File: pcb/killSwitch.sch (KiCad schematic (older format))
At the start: 8 parts

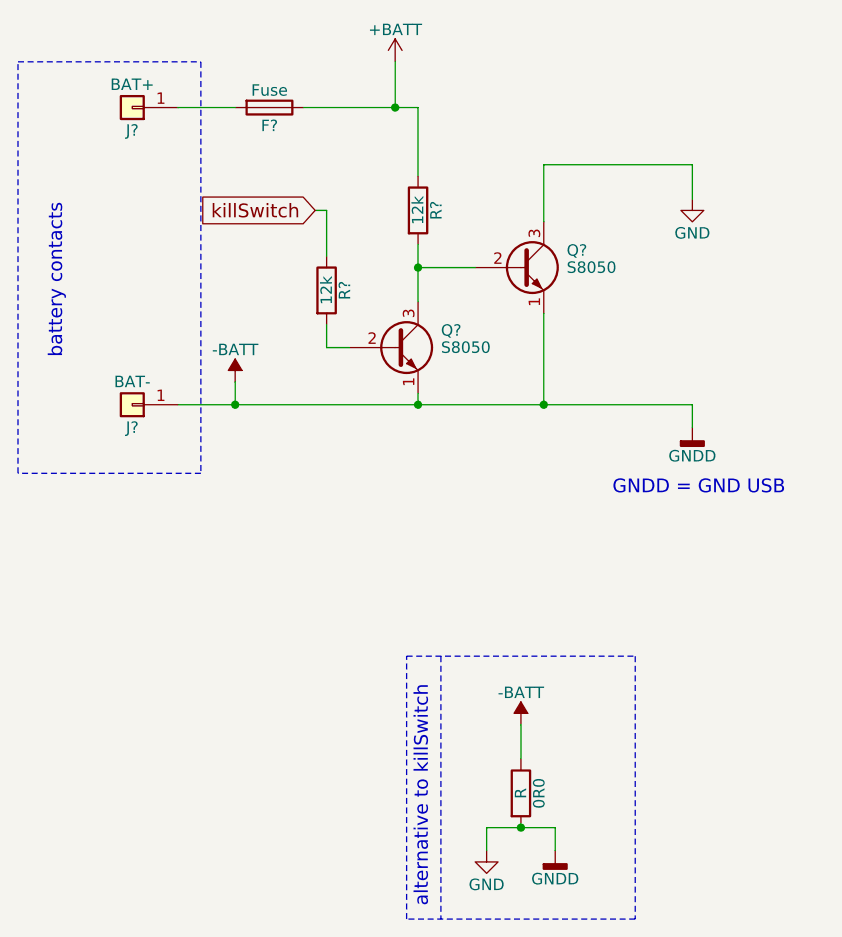
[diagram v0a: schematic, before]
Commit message: nightly | pcb build, routing, placing
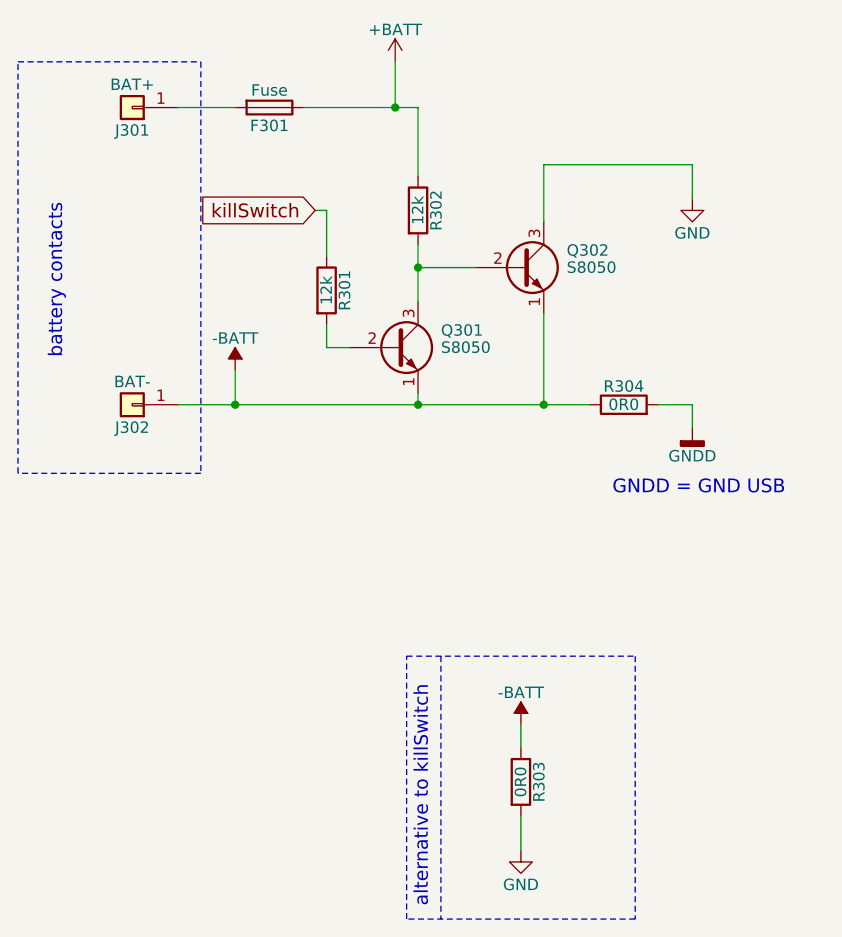
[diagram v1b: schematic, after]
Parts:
- added R304: 0R0, Resistors_SMD:R_0603_HandSoldering, symbol R
- F301: renamed from F?; footprint (none) -> SMD_Packages:SMD-1210_Pol
- J301, J302: renamed from J?; footprint (none) -> Wire_Pads:SolderWirePad_single_SMD_5x10mm
- Q301, Q302: renamed from Q?; footprint TO_SOT_Packages_THT:TO-92_Molded_Narrow -> TO_SOT_Packages_SMD:SOT-23_Handsoldering
- R301, R302: renamed from R?; footprint (none) -> Resistors_SMD:R_0603_HandSoldering
- R303: renamed from 0R0; value R -> 0R0; footprint (none) -> Resistors_SMD:R_0603_HandSoldering
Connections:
- net -BATT: now also R304.1; no longer Q302.3 (C), R303.2
- new net GND: Q302.3 (C), R303.2
- new net GNDD: R304.2
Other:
- moved on the sheet: R303
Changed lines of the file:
@@
 LIBS:contrib
 LIBS:valves
-LIBS:MC34063
 LIBS:adxl345
+LIBS:ws2812b
 LIBS:fantimote-cache
 EELAYER 25 0
@@
 $Descr A4 11693 8268
 encoding utf-8
-Sheet 3 7
+Sheet 3 10
 Title "seniorsRemote (fantimote)"
 Date "2018-07-07"
@@
 $EndDescr
 $Comp
-L Conn_01x01 J?
+L Conn_01x01 J301
 U 1 1 5B40C4B5
 P 2050 1550
-F 0 "J?" H 2050 1650 50  0000 C CNN
+F 0 "J301" H 2050 1650 50  0000 C CNN
 F 1 "BAT+" H 2050 1450 50  0000 C CNN
-F 2 "" H 2050 1550 50  0001 C CNN
+F 2 "Wire_Pads:SolderWirePad_single_SMD_5x10mm" H 2050 1550 50  0001 C CNN
 F 3 "" H 2050 1550 50  0001 C CNN
 	1    2050 1550
@@
 $EndComp
 $Comp
-L Conn_01x01 J?
+L Conn_01x01 J302
 U 1 1 5B40C51B
 P 2050 2850
-F 0 "J?" H 2050 2950 50  0000 C CNN
+F 0 "J302" H 2050 2950 50  0000 C CNN
 F 1 "BAT-" H 2050 2750 50  0000 C CNN
-F 2 "" H 2050 2850 50  0001 C CNN
+F 2 "Wire_Pads:SolderWirePad_single_SMD_5x10mm" H 2050 2850 50  0001 C CNN
 F 3 "" H 2050 2850 50  0001 C CNN
 	1    2050 2850
@@
 $EndComp
 $Comp
-L Fuse F?
+L Fuse F301
 U 1 1 5B40C629
 P 2650 1550
-F 0 "F?" V 2730 1550 50  0000 C CNN
+F 0 "F301" V 2730 1550 50  0000 C CNN
 F 1 "Fuse" V 2575 1550 50  0000 C CNN
-F 2 "" V 2580 1550 50  0001 C CNN
+F 2 "SMD_Packages:SMD-1210_Pol" V 2580 1550 50  0001 C CNN
 F 3 "" H 2650 1550 50  0001 C CNN
 	1    2650 1550
@@
 	2250 1550 2500 1550
 $Comp
-L S8050 Q?
+L S8050 Q302
 U 1 1 5B40C65D
 P 3750 2250
-F 0 "Q?" H 3950 2325 50  0000 L CNN
+F 0 "Q302" H 3950 2325 50  0000 L CNN
 F 1 "S8050" H 3950 2250 50  0000 L CNN
-F 2 "TO_SOT_Packages_THT:TO-92_Molded_Narrow" H 3950 2175 50  0001 L CIN
+F 2 "TO_SOT_Packages_SMD:SOT-23_Handsoldering" H 3950 2175 50  0001 L CIN
 F 3 "" H 3750 2250 50  0001 L CNN
 	1    3750 2250
@@
 	3300 2250 3550 2250
 Wire Wire Line
-	2250 2850 4500 2850
-Wire Wire Line
 	3850 2850 3850 2450
 $Comp
-L GND #PWR?
+L GND #PWR014
 U 1 1 5B40C700
 P 4500 1950
-F 0 "#PWR?" H 4500 1700 50  0001 C CNN
+F 0 "#PWR014" H 4500 1700 50  0001 C CNN
 F 1 "GND" H 4500 1800 50  0000 C CNN
 F 2 "" H 4500 1950 50  0001 C CNN
@@
 	4500 1800 4500 1950
 $Comp
-L GNDD #PWR?
+L GNDD #PWR015
 U 1 1 5B40C727
 P 4500 2950
-F 0 "#PWR?" H 4500 2700 50  0001 C CNN
+F 0 "#PWR015" H 4500 2700 50  0001 C CNN
 F 1 "GNDD" H 4500 2825 50  0000 C CNN
 F 2 "" H 4500 2950 50  0001 C CNN
@@
 GNDD = GND USB\n
 $Comp
-L +BATT #PWR?
+L +BATT #PWR016
 U 1 1 5B40C788
 P 3200 1350
-F 0 "#PWR?" H 3200 1200 50  0001 C CNN
+F 0 "#PWR016" H 3200 1200 50  0001 C CNN
 F 1 "+BATT" H 3200 1490 50  0000 C CNN
 F 2 "" H 3200 1350 50  0001 C CNN
@@
 	2800 1550 3300 1550
 $Comp
-L -BATT #PWR?
+L -BATT #PWR017
 U 1 1 5B40C86C
-P 2500 2750
-F 0 "#PWR?" H 2500 2600 50  0001 C CNN
-F 1 "-BATT" H 2500 2890 50  0000 C CNN
-F 2 "" H 2500 2750 50  0001 C CNN
-F 3 "" H 2500 2750 50  0001 C CNN
-	1    2500 2750
-	1    0    0    -1
-$EndComp
-Wire Wire Line
-	2500 2750 2500 2850
+P 2500 2700
+F 0 "#PWR017" H 2500 2550 50  0001 C CNN
+F 1 "-BATT" H 2500 2840 50  0000 C CNN
+F 2 "" H 2500 2700 50  0001 C CNN
+F 3 "" H 2500 2700 50  0001 C CNN
+	1    2500 2700
+	1    0    0    -1
+$EndComp
+Wire Wire Line
+	2500 2700 2500 2850
 Connection ~ 2500 2850
 $Comp
-L -BATT #PWR?
+L -BATT #PWR018
 U 1 1 5B40C8AA
 P 3750 4250
-F 0 "#PWR?" H 3750 4100 50  0001 C CNN
+F 0 "#PWR018" H 3750 4100 50  0001 C CNN
 F 1 "-BATT" H 3750 4390 50  0000 C CNN
 F 2 "" H 3750 4250 50  0001 C CNN
@@
 $EndComp
 $Comp
-L GND #PWR?
+L GND #PWR019
 U 1 1 5B40C8C6
-P 3600 4800
-F 0 "#PWR?" H 3600 4550 50  0001 C CNN
-F 1 "GND" H 3600 4650 50  0000 C CNN
-F 2 "" H 3600 4800 50  0001 C CNN
-F 3 "" H 3600 4800 50  0001 C CNN
-	1    3600 4800
-	1    0    0    -1
-$EndComp
-$Comp
-L GNDD #PWR?
-U 1 1 5B40C8E2
-P 3900 4800
-F 0 "#PWR?" H 3900 4550 50  0001 C CNN
-F 1 "GNDD" H 3900 4675 50  0000 C CNN
-F 2 "" H 3900 4800 50  0001 C CNN
-F 3 "" H 3900 4800 50  0001 C CNN
-	1    3900 4800
-	1    0    0    -1
-$EndComp
-$Comp
-L R 0R0
+P 3750 4800
+F 0 "#PWR019" H 3750 4550 50  0001 C CNN
+F 1 "GND" H 3750 4650 50  0000 C CNN
+F 2 "" H 3750 4800 50  0001 C CNN
+F 3 "" H 3750 4800 50  0001 C CNN
+	1    3750 4800
+	1    0    0    -1
+$EndComp
+$Comp
+L R R303
 U 1 1 5B40C8FE
-P 3750 4550
-F 0 "0R0" V 3830 4550 50  0000 C CNN
-F 1 "R" V 3750 4550 50  0000 C CNN
-F 2 "" V 3680 4550 50  0001 C CNN
-F 3 "" H 3750 4550 50  0001 C CNN
-	1    3750 4550
-	1    0    0    -1
-$EndComp
-Wire Wire Line
-	3750 4250 3750 4400
-Wire Wire Line
-	3600 4700 3900 4700
-Wire Wire Line
-	3900 4700 3900 4800
-Wire Wire Line
-	3600 4700 3600 4800
-Connection ~ 3750 4700
+P 3750 4500
+F 0 "R303" V 3830 4500 50  0000 C CNN
+F 1 "0R0" V 3750 4500 50  0000 C CNN
+F 2 "Resistors_SMD:R_0603_HandSoldering" V 3680 4500 50  0001 C CNN
+F 3 "" H 3750 4500 50  0001 C CNN
+	1    3750 4500
+	1    0    0    -1
+$EndComp
+Wire Wire Line
+	3750 4250 3750 4350
+Wire Wire Line
+	3750 4650 3750 4800
 Wire Notes Line
 	3250 3950 4250 3950
@@
 battery contacts
 $Comp
-L R R?
+L R R302
 U 1 1 5B40CA5D
 P 3300 2000
-F 0 "R?" V 3380 2000 50  0000 C CNN
+F 0 "R302" V 3380 2000 50  0000 C CNN
 F 1 "12k" V 3300 2000 50  0000 C CNN
-F 2 "" V 3230 2000 50  0001 C CNN
+F 2 "Resistors_SMD:R_0603_HandSoldering" V 3230 2000 50  0001 C CNN
 F 3 "" H 3300 2000 50  0001 C CNN
 	1    3300 2000
@@
 Connection ~ 3300 2250
 $Comp
-L R R?
+L R R301
 U 1 1 5B40CB3C
 P 2900 2350
-F 0 "R?" V 2980 2350 50  0000 C CNN
+F 0 "R301" V 2980 2350 50  0000 C CNN
 F 1 "12k" V 2900 2350 50  0000 C CNN
-F 2 "" V 2830 2350 50  0001 C CNN
+F 2 "Resistors_SMD:R_0603_HandSoldering" V 2830 2350 50  0001 C CNN
 F 3 "" H 2900 2350 50  0001 C CNN
 	1    2900 2350
@@
 $EndComp
 $Comp
-L S8050 Q?
+L S8050 Q301
 U 1 1 5B40CC60
 P 3200 2600
-F 0 "Q?" H 3400 2675 50  0000 L CNN
+F 0 "Q301" H 3400 2675 50  0000 L CNN
 F 1 "S8050" H 3400 2600 50  0000 L CNN
-F 2 "TO_SOT_Packages_THT:TO-92_Molded_Narrow" H 3400 2525 50  0001 L CIN
+F 2 "TO_SOT_Packages_SMD:SOT-23_Handsoldering" H 3400 2525 50  0001 L CIN
 F 3 "" H 3200 2600 50  0001 L CNN
 	1    3200 2600
@@
 $EndComp
 Wire Wire Line
-	3300 2800 3300 2850
+	3300 2850 3300 2800
 Connection ~ 3300 2850
 Wire Wire Line
@@
 Wire Wire Line
 	2900 2000 2900 2200
+Wire Wire Line
+	2250 2850 4050 2850
+$Comp
+L R R304
+U 1 1 5B43DD94
+P 4200 2850
+F 0 "R304" V 4280 2850 50  0000 C CNN
+F 1 "0R0" V 4200 2850 50  0000 C CNN
+F 2 "Resistors_SMD:R_0603_HandSoldering" V 4130 2850 50  0001 C CNN
+F 3 "" H 4200 2850 50  0001 C CNN
+	1    4200 2850
+	0    -1   -1   0
+$EndComp
+Wire Wire Line
+	4350 2850 4500 2850
 $EndSCHEMATC
